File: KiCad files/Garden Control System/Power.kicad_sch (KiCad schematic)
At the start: 0 parts

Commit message: working on power arch
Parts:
- added R16, R7: RB051LAM-40TR, DIO_RB050LAM_ROM, symbol rb051lam-40tr:RB051LAM-40TR
- added R17: R_Shunt, symbol Device:R_Shunt
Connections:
- new net I_SENSE3_+: R17.3
- new net I_SENSE3_-: R17.2
- new net USB_VBUS: R16.1
- new net VBAT: R7.1
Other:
- note added: "BEST WAY TO GO FROM 12-18V-5.5MAX FOR LDO SUPPLY BUCK: BD9227F-E2 LDO: LP38511MRX-ADJ/NOPB"
- note added: "COULD REDUCE CURRENT RATING OF DIODE"

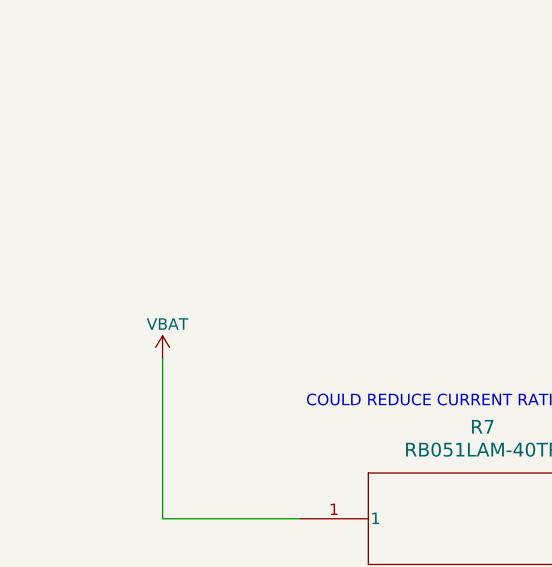
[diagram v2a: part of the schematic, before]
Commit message: working on gate driver circuit for motor control
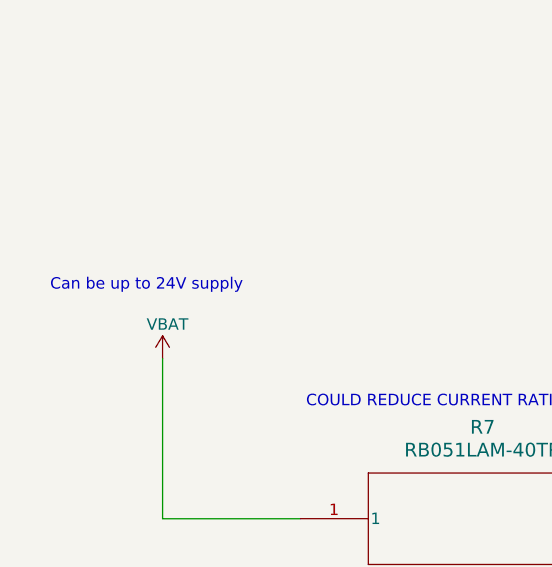
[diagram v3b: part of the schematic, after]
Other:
- note added: "Can be up to 24V supply"
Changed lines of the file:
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@@
+		)
+	)
+	(text "Can be up to 24V supply"
+		(exclude_from_sim no)
+		(at 43.942 79.502 0)
+		(effects
+			(font
+				(size 1.27 1.27)
+				(color 255 0 0 1)
+			)
 		)
 	)

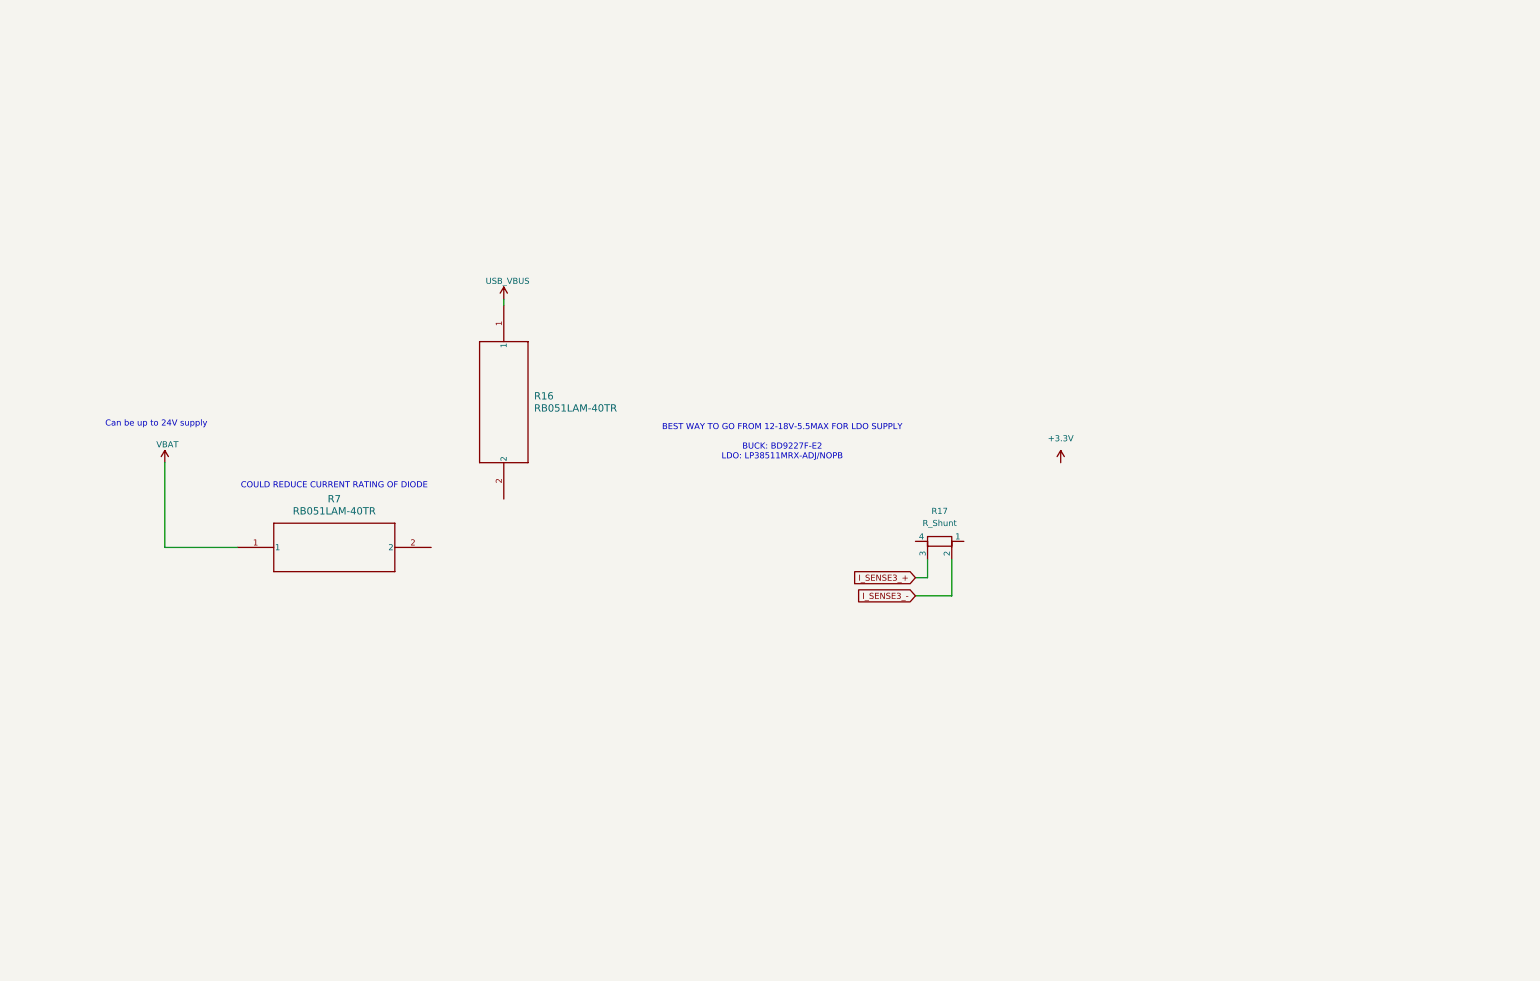
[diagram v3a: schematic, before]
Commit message: expanded power supply section. completed LSD design. sized shunt resistors
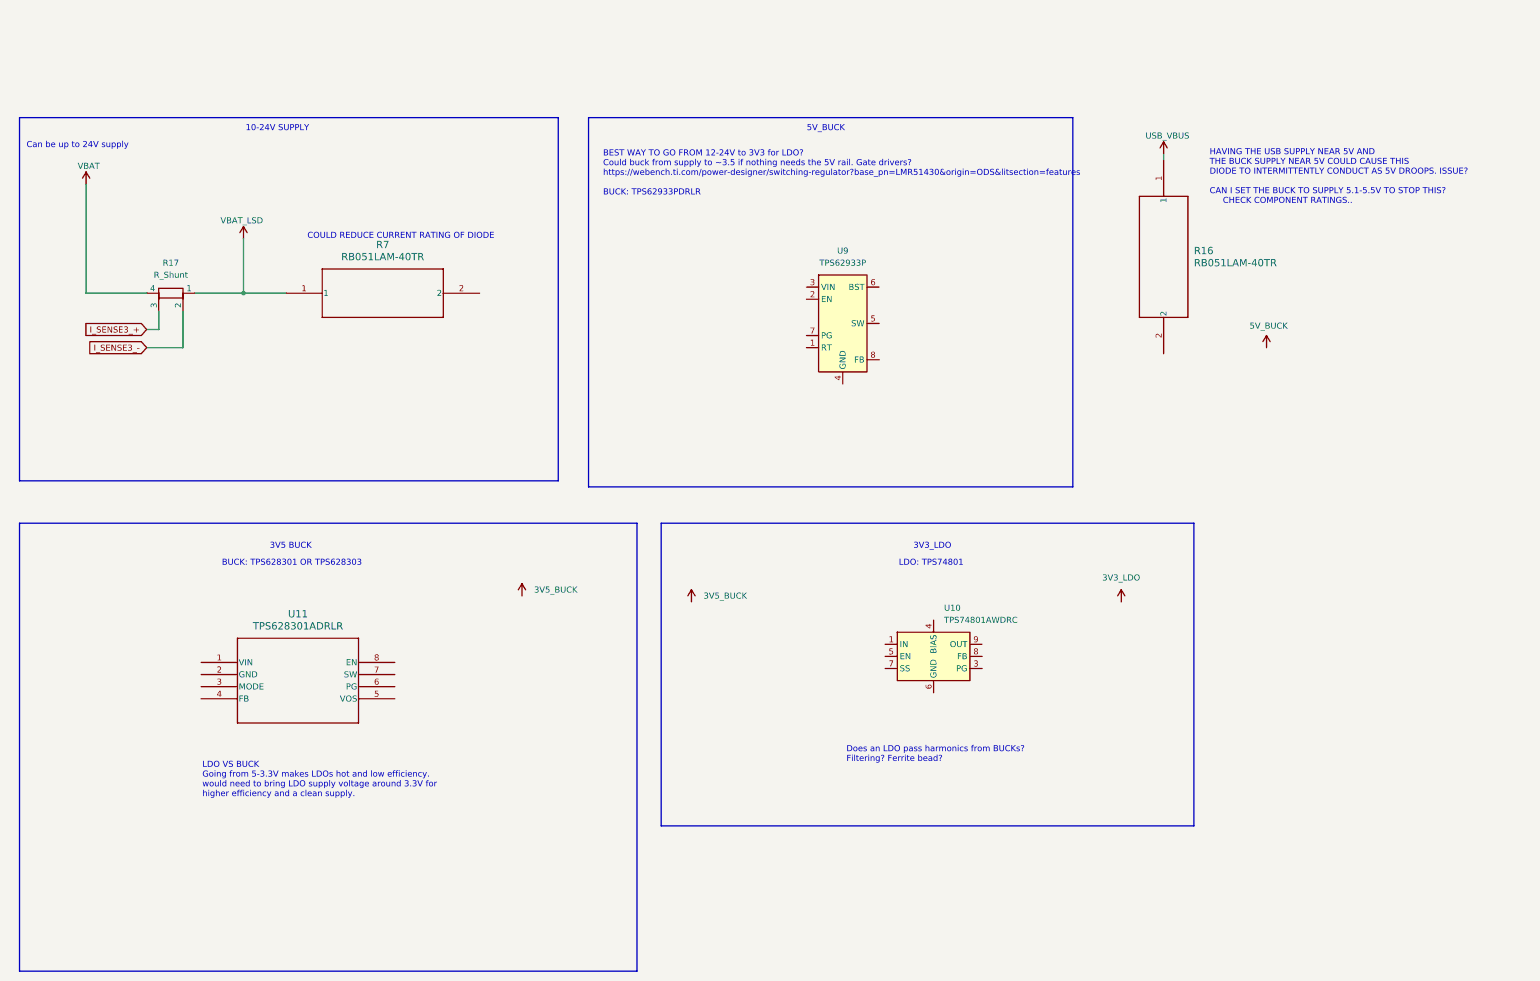
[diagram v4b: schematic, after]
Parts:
- added U10: TPS74801AWDRC, Package_SON:VSON-10-1EP_3x3mm_P0.5mm_EP1.65x2.4mm_ThermalVias, symbol Regulator_Linear:TPS74801AWDRC
- added U11: TPS628301ADRLR, DRL0008A_TPS628301ADRLR_TEX, symbol TPS628301ADRLR:TPS628301ADRLR
- added U9: TPS62933P, Package_TO_SOT_SMD:SOT-583-8, symbol Regulator_Switching:TPS62933P
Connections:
- net VBAT: now also R17.4; no longer R7.1
- net VBAT_LSD: now reaches R17.1
- net VBAT_LSD: now also R7.1
- new net: U10.1 (IN), U10.2 (IN)
- new net: U10.10 (OUT), U10.9 (OUT)
- new net: U10.11 (GND), U10.6 (GND)
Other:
- note added: "10-24V SUPPLY"
- note added: "3V3_LDO"
- note added: "3V5 BUCK"
- note added: "5V_BUCK"
- note added: "BEST WAY TO GO FROM 12-24V to 3V3 for LDO? Could buck from supply to ~3.5 if nothing needs the 5V rail. Gate drivers? https://webench.ti.com/power-designer/switching-regulator?base_pn=LMR51430&origin=ODS&litsection=features BUCK: TPS62933PDRLR"
- note added: "BUCK: TPS628301 OR TPS628303"
- note added: "Does an LDO pass harmonics from BUCKs? Filtering? Ferrite bead?"
- note added: "HAVING THE USB SUPPLY NEAR 5V AND THE BUCK SUPPLY NEAR 5V COULD CAUSE THIS DIODE TO INTERMITTENTLY CONDUCT AS 5V DROOPS. ISSUE? CAN I SET THE BUCK TO SUPPLY 5.1-5.5V TO STOP THIS? CHECK COMPONENT RATINGS.."
- note added: "LDO VS BUCK Going from 5-3.3V makes LDOs hot and low efficiency. would need to bring LDO supply voltage around 3.3V for higher efficiency and a clean supply."
- note added: "LDO: TPS74801"
- note removed: "BEST WAY TO GO FROM 12-18V-5.5MAX FOR LDO SUPPLY BUCK: BD9227F-E2 LDO: LP38511MRX-ADJ/NOPB"
- moved on the sheet: R16, R17, R7

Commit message: adding recent schematic progress
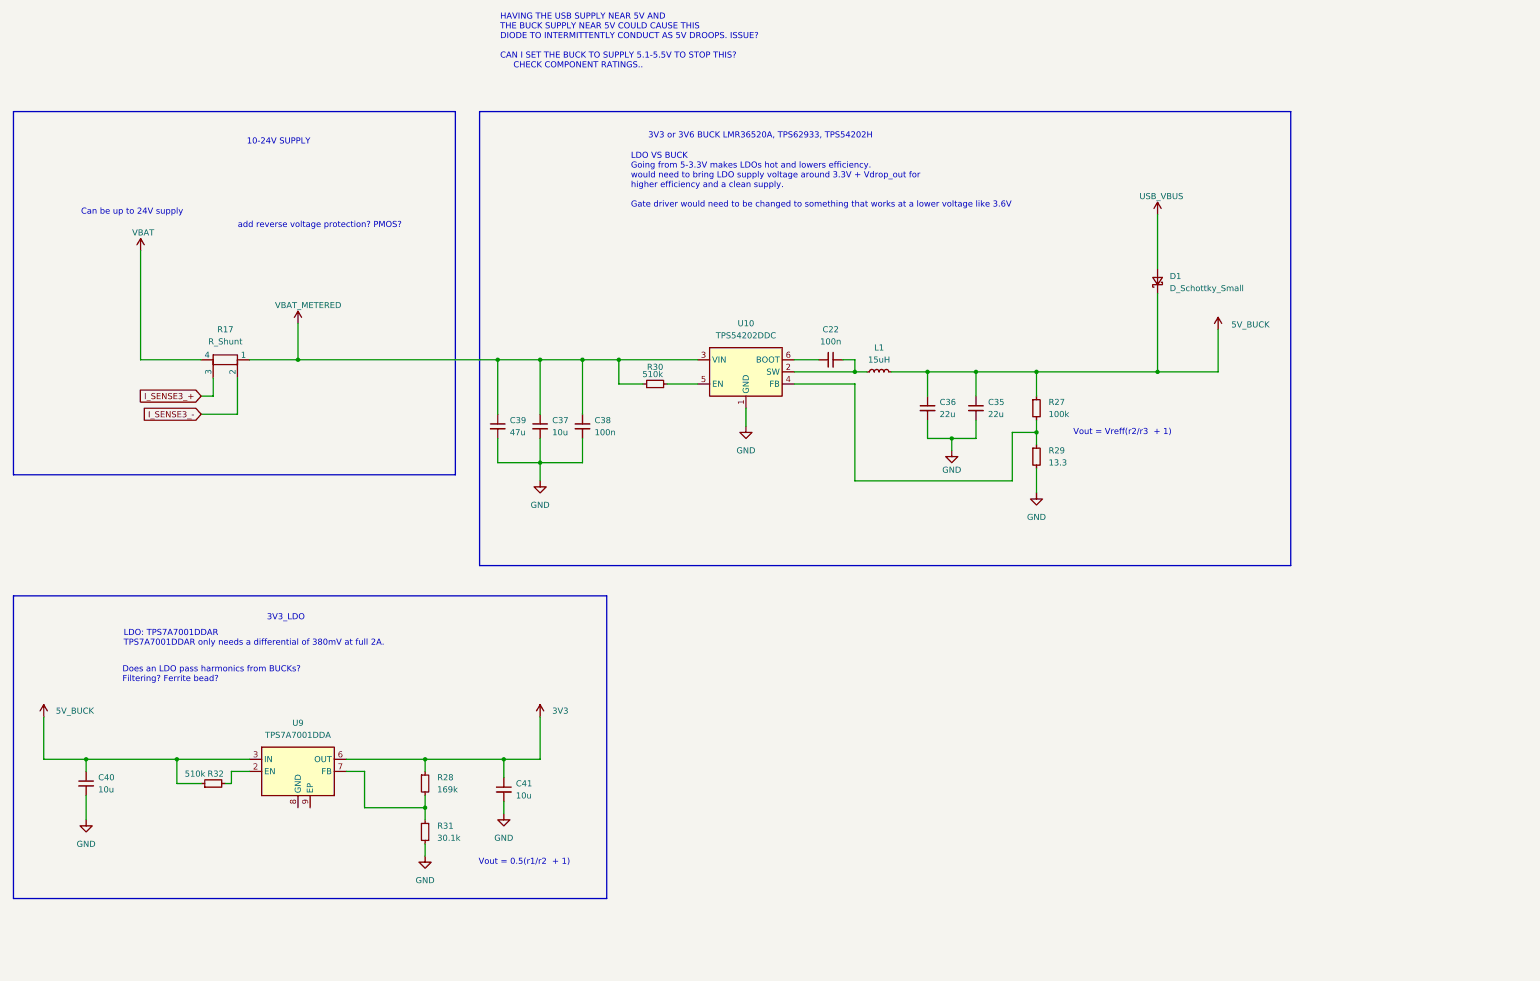
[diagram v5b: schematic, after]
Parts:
- removed R16, R7: RB051LAM-40TR, DIO_RB050LAM_ROM, symbol rb051lam-40tr:RB051LAM-40TR
- removed U10: TPS74801AWDRC, Package_SON:VSON-10-1EP_3x3mm_P0.5mm_EP1.65x2.4mm_ThermalVias, symbol Regulator_Linear:TPS74801AWDRC
- removed U11: TPS628301ADRLR, DRL0008A_TPS628301ADRLR_TEX, symbol TPS628301ADRLR:TPS628301ADRLR
- removed U9: TPS62933P, Package_TO_SOT_SMD:SOT-583-8, symbol Regulator_Switching:TPS62933P
- added C22, C38: 100n, symbol Device:C_Small
- added C35, C36: 22u, symbol Device:C_Small
- added C37, C40, C41: 10u, symbol Device:C_Small
- added C39: 47u, symbol Device:C_Small
- added D1: D_Schottky_Small, symbol Device:D_Schottky_Small
- added L1: 15uH, symbol Device:L_Small
- added R27: 100k, symbol Device:R_Small
- added R28: 169k, symbol Device:R_Small
- added R29: 13.3, symbol Device:R_Small
- added R30, R32: 510k, symbol Device:R_Small
- added R31: 30.1k, symbol Device:R_Small
- added U10: TPS54202DDC, Package_TO_SOT_SMD:SOT-23-6, symbol Regulator_Switching:TPS54202DDC
- added U9: TPS7A7001DDA, Package_SO:TI_SO-PowerPAD-8, symbol Regulator_Linear:TPS7A7001DDA
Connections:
- net 5V_BUCK: now also C35.1, C36.1, C40.1, D1.1 (K), L1.2, R27.1, R32.1, U9.3 (IN)
- net USB_VBUS: now also D1.2 (A)
- net VBAT_LSD renamed VBAT_METERED
- net VBAT_METERED: now also C37.1, C38.1, C39.1, R30.1, U10.3 (VIN)
- new net: C22.2, L1.1, U10.2 (SW)
- new net: R32.2, U9.2 (EN)
- new net: R28.2, R31.1, U9.7 (FB)
- new net: C22.1, U10.6 (BOOT)
- new net: R30.2, U10.5 (EN)
- new net: R27.2, R29.1, U10.4 (FB)
- new net 3V3: C41.1, R28.1, U9.6 (OUT)
- new net GND: C35.2, C36.2, C37.2, C38.2, C39.2, C40.2, C41.2, R29.2, R31.2, U10.1 (GND)
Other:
- note added: "3V3 or 3V6 BUCK LMR36520A, TPS62933, TPS54202H"
- note added: "LDO VS BUCK Going from 5-3.3V makes LDOs hot and lowers efficiency. would need to bring LDO supply voltage around 3.3V + Vdrop_out for higher efficiency and a clean supply. Gate driver would need to be changed to something that works at a lower voltage like 3.6V"
- note added: "LDO: TPS7A7001DDAR TPS7A7001DDAR only needs a differential of 380mV at full 2A."
- note added: "Vout = 0.5(r1/r2 + 1)"
- note added: "Vout = Vreff(r2/r3 + 1)"
- note added: "add reverse voltage protection? PMOS?"
- note removed: "3V5 BUCK"
- note removed: "5V_BUCK"
- note removed: "BEST WAY TO GO FROM 12-24V to 3V3 for LDO? Could buck from supply to ~3.5 if nothing needs the 5V rail. Gate drivers? https://webench.ti.com/power-designer/switching-regulator?base_pn=LMR51430&origin=ODS&litsection=features BUCK: TPS62933PDRLR"
- note removed: "BUCK: TPS628301 OR TPS628303"
- note removed: "COULD REDUCE CURRENT RATING OF DIODE"
- note removed: "LDO VS BUCK Going from 5-3.3V makes LDOs hot and low efficiency. would need to bring LDO supply voltage around 3.3V for higher efficiency and a clean supply."
- note removed: "LDO: TPS74801"
- moved on the sheet: R17

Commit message: working on temp sensor circuit
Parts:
- added D2: 5V LED, symbol Device:LED_Small
- added D3: 3V3 LED, symbol Device:LED_Small
- added R37: 3k16, symbol Device:R_Small
- added R38: 1k47, symbol Device:R_Small
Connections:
- net 3V3: now also D3.2 (A)
- net 5V_BUCK: now also D2.2 (A)
- net GND: now also R37.2, R38.2
- new net: D2.1 (K), R37.1
- new net: D3.1 (K), R38.1
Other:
- note added: "LED SML-P11UTT86R Vfw = 1.8, I = 1mA"

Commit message: Added a basic readme
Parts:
- added C49, C50: 100n, symbol Device:C_Small
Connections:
- net 3V3: now also C50.1
- net 5V_BUCK: now also C49.1
- net GND: now also C49.2, C50.2
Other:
- moved on the sheet: C41
